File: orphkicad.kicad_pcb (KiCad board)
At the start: 2 copper layers, 21 x 51 mm, 43 parts, among them J1 USB_C_Receptacle_USB2.0_16P, J2 SWD, SW1 BTN_BOOT, SW2 BTN_RST, SW3 BTN_USR, U1 RP2040, U2 W25Q16JVUXIQ, U3 USBLC6-2SC6, U5 XC6206PxxxMR, X1 X322512MOB4SI 12pF

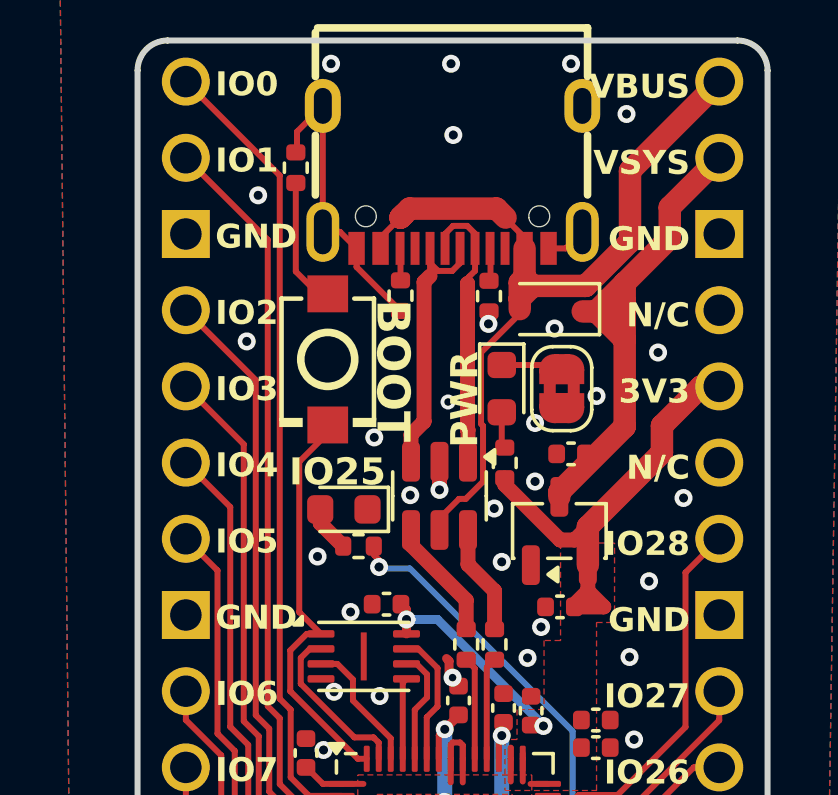
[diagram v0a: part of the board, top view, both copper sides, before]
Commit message: Move BOOT label
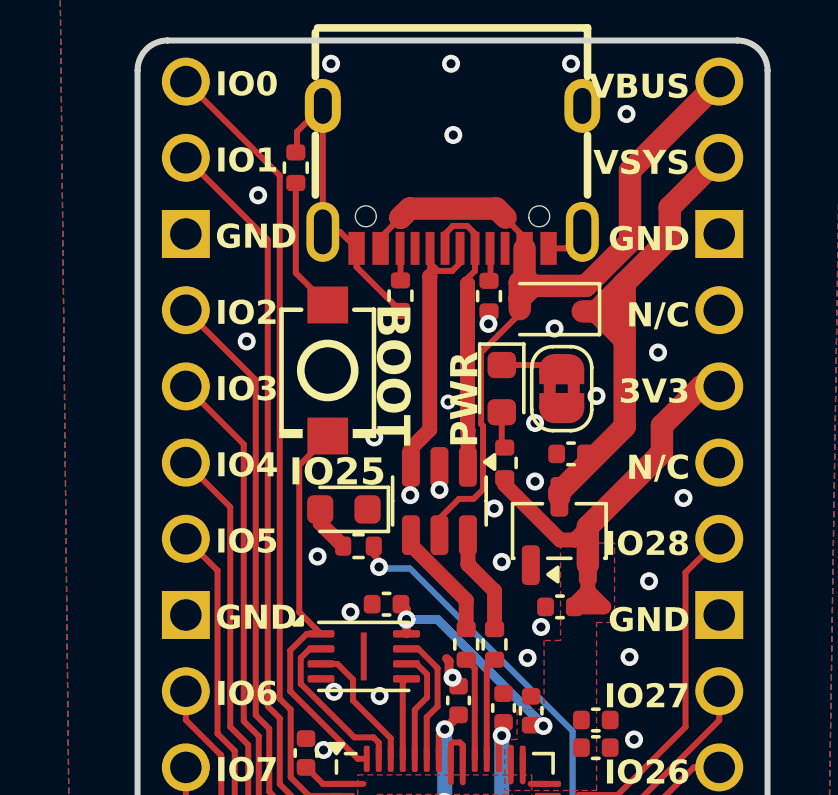
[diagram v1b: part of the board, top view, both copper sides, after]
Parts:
- moved SW1 0.37 mm to (56.3, 41.0)
- moved U3 0.17 mm to (60.1, 45.4)
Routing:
- net USB_DP: vias 0 -> 1
- net GND: vias 67 -> 66

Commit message: Remove extra space from LCSC Part #
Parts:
- R3, R4: value 27R -> 33R
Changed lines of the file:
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@@
 			)
 		)
-		(property "LCSC" "C455280 "
+		(property "LCSC" "C455280"
 			(at 0 0 270)
 			(unlocked yes)
@@
 			)
 		)
-		(property "Value" "27R"
+		(property "Value" "33R"
 			(at 0 1.17 90)
 			(layer "F.Fab")
@@
 			)
 		)
-		(property "LCSC" "C2909343"
+		(property "LCSC" "C25105"
 			(at 0 0 0)
 			(layer "F.SilkS")
@@
 			)
 		)
-		(property "LCSC" "C2765186 "
+		(property "LCSC" "C2765186"
 			(at 0 0 0)
 			(layer "F.SilkS")
@@
 			)
 		)
-		(property "LCSC" "C455280 "
+		(property "LCSC" "C455280"
 			(at 0 0 0)
 			(layer "F.SilkS")
@@
 			)
 		)
-		(property "LCSC" "C455280 "
+		(property "LCSC" "C455280"
 			(at 0 0 90)
 			(unlocked yes)
@@
 			)
 		)
-		(property "Value" "27R"
+		(property "Value" "33R"
 			(at 0 1.17 90)
 			(layer "F.Fab")
@@
 			)
 		)
-		(property "LCSC" "C2909343"
+		(property "LCSC" "C25105"
 			(at 0 0 0)
 			(layer "F.SilkS")
